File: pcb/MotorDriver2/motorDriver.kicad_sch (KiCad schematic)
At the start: 22 parts, among them Q2 IRLZ44NSTRLPBF, Q3 IRLZ44NSTRLPBF, Q4 IRLZ44NSTRLPBF, Q5 IRLZ44NSTRLPBF

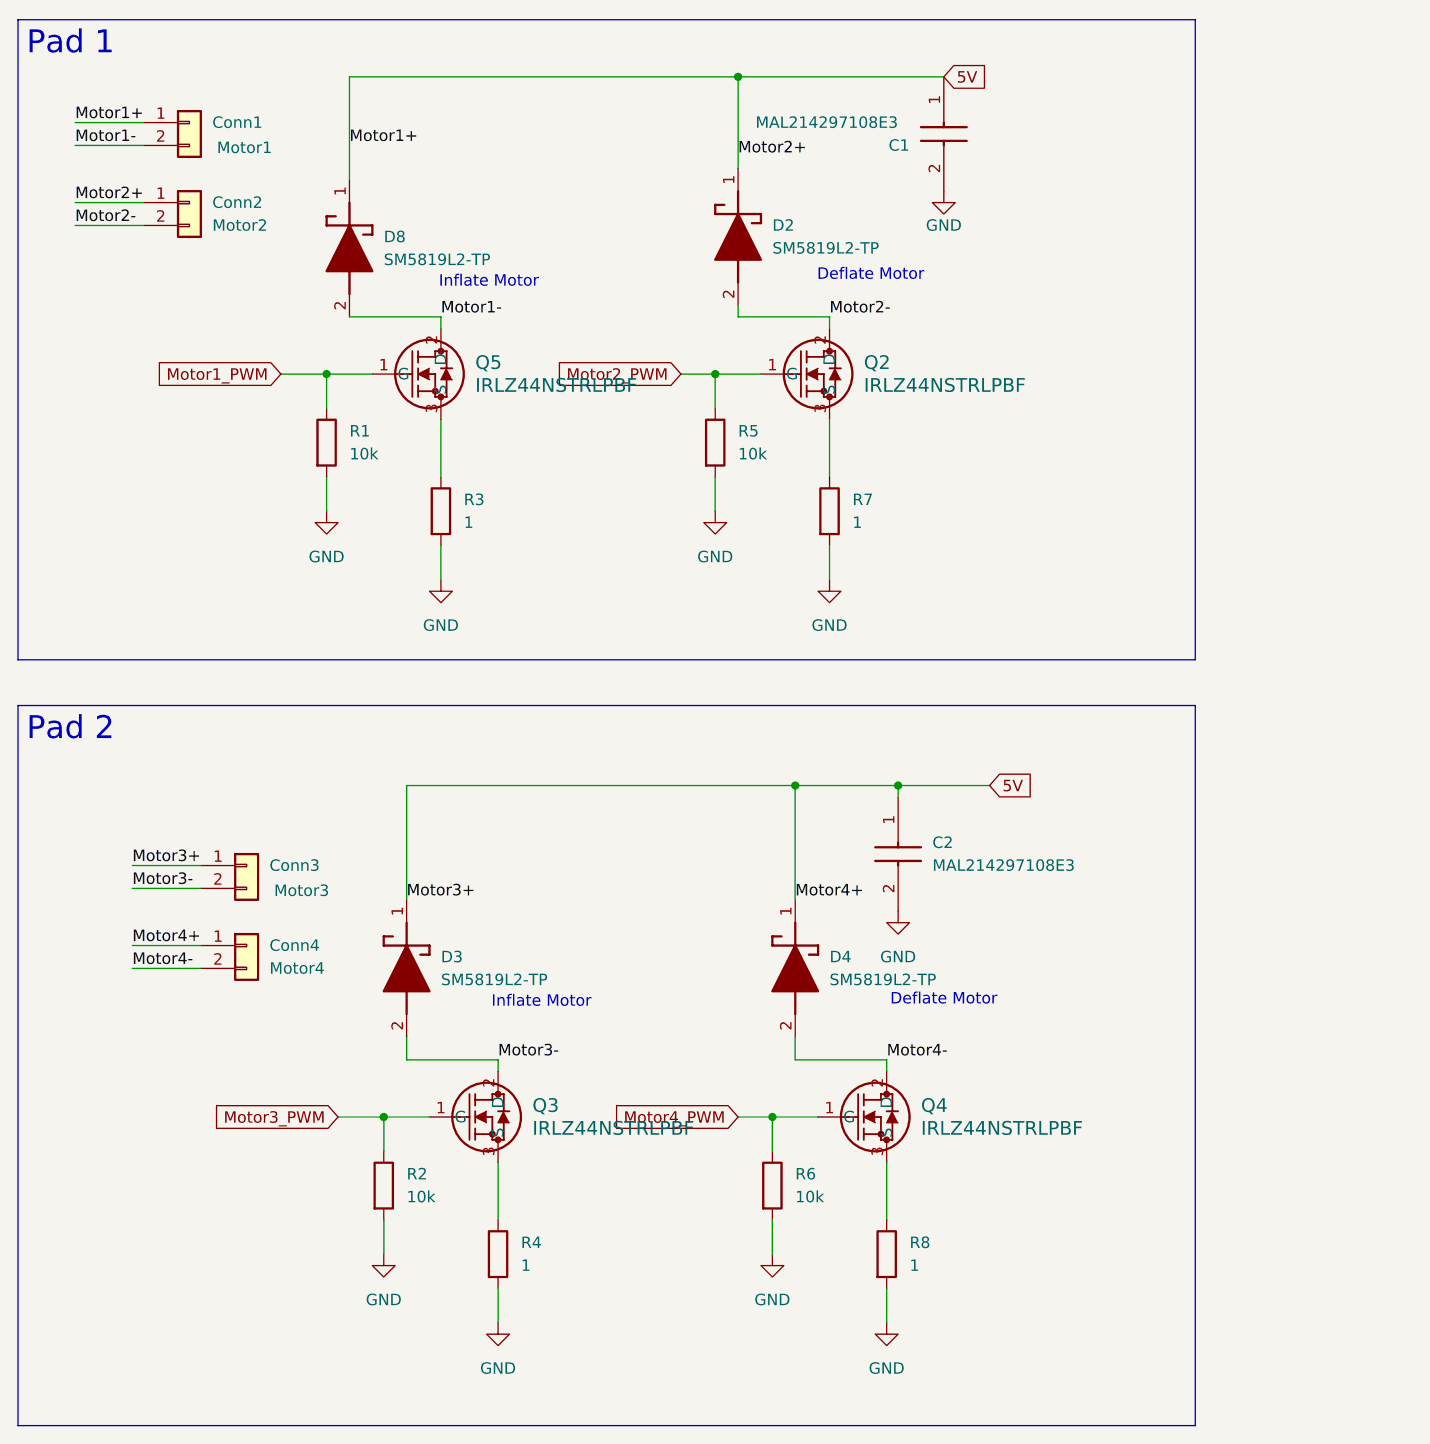
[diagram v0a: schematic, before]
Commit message: Modified pwm pins
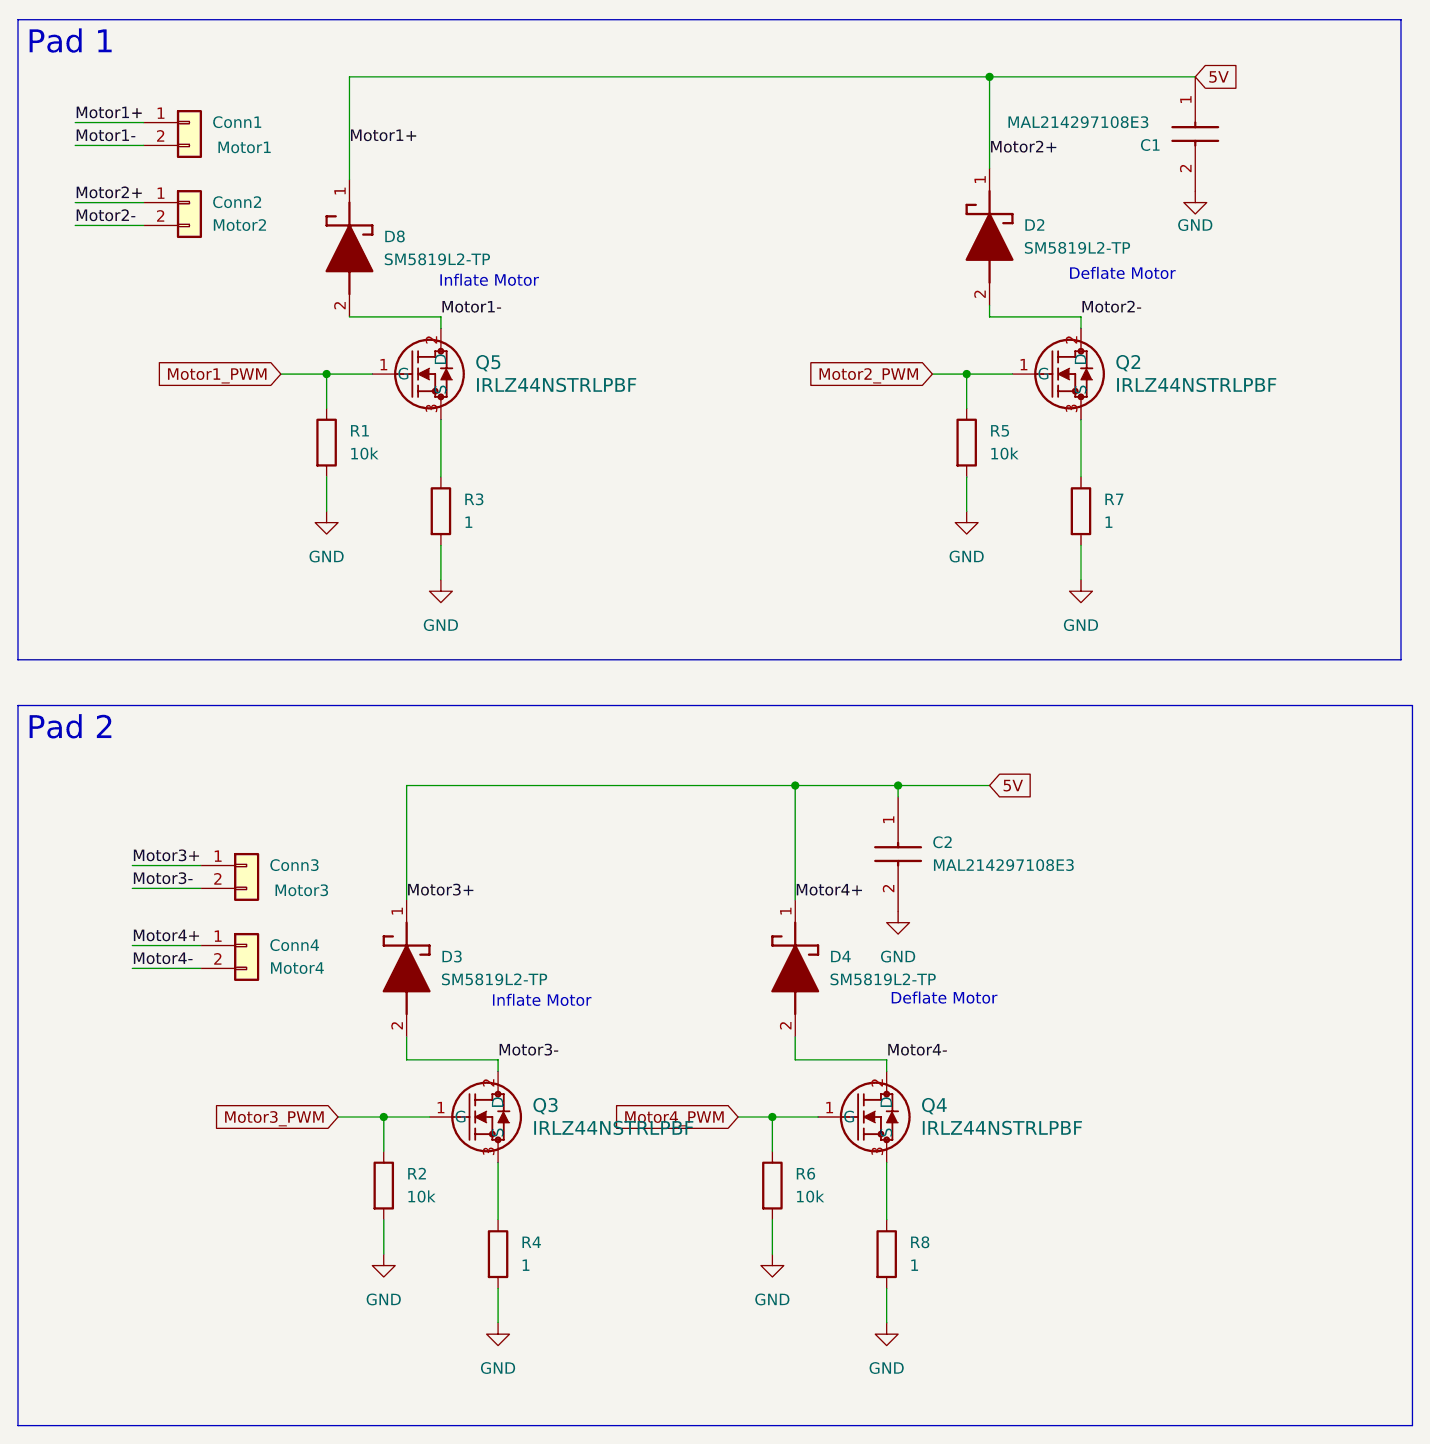
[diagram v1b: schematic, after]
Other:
- moved on the sheet: C1, D2, Q2, R5, R7

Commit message: Laying out PCB
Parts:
- removed D8: SM5819L2-TP, footprintLib:SDO_SM5819L2-TP_MCE, symbol pcb:SM5819L2-TP
- removed Q5: IRLZ44NSTRLPBF, footprintLib:NMOSGDS_D2PAK_INF, symbol pcb:IRLZ44NSTRLPBF
- removed R1: 10k, Resistor_SMD:R_0402_1005Metric, symbol Device:R
- removed R3: 1, Resistor_SMD:R_1206_3216Metric, symbol Device:R
- added D12: SM5819L2-TP, CapstoneFootprints:SDO_SM5819L2-TP_MCE, symbol pcb:SM5819L2-TP
- added Q6: IRLZ44NSTRLPBF, CapstoneFootprints:NMOSGDS_D2PAK_INF, symbol pcb:IRLZ44NSTRLPBF
- added R38: 10k, Resistor_SMD:R_0402_1005Metric, symbol Device:R
- added R40: 1, Resistor_SMD:R_1206_3216Metric, symbol Device:R
- C1, C2: value MAL214297108E3 -> Honor Elec RVT1H470M0607; footprint footprintLib:CAPAE680X800N -> CapstoneFootprints:CAPAE680X800N
- D2, D3, D4: footprint footprintLib:SDO_SM5819L2-TP_MCE -> CapstoneFootprints:SDO_SM5819L2-TP_MCE
- Q2, Q3, Q4: footprint footprintLib:NMOSGDS_D2PAK_INF -> CapstoneFootprints:NMOSGDS_D2PAK_INF
- R4, R7, R8: LCSC (none) -> C17928
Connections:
- net 5V: now also D12.1 (K)
- net GND: now also R38.2, R40.2
- net Motor1- renamed Motor1a-
- net Motor1a-: now also D3.2 (A), Q3.2 (D)
- net Motor2- renamed Motor1b-
- net Motor2_PWM renamed Motor1b_PWM
- removed net Motor3-: Conn3.2 (Pin_2), D3.2 (A), Q3.2 (D)
- net Motor3_PWM renamed Motor1a_PWM
- net Motor4- renamed Motor2b-
- net Motor4_PWM renamed Motor2b_PWM
- new net: Q6.3 (S), R40.1
- new net Motor2a-: Conn3.2 (Pin_2), D12.2 (A), Q6.2 (D)
- new net Motor2a_PWM: Q6.1 (G), R38.1
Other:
- moved on the sheet: Conn1, Conn2, Conn3, Conn4, D3, Q3, R2, R4
